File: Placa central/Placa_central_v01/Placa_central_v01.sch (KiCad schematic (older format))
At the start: 69 parts, among them J1 PinoCheckBateriaVcc, J10 Conn_01x01_Arduino11, J11 Conn_01x01_Arduino12, J12 Conn_01x01_Arduino13, J13 Conn_01x01_Arduino14, J14 Conn_01x01_Arduino15, J15 Conn_01x01_Arduino16, J16 Conn_01x01_Motor1PonteHPCB, J17 PinoChargeBateriaGND, J18 Conn_01x01_Arduino19, J19 Conn_01x01_Arduino20, J2 Conn_01x02_ArduinoTxRx, J20 Conn_01x01_Arduino21, J21 Conn_01x01_Arduino22, J22 Conn_01x01_Arduino23, J23 Conn_01x01_Arduino24, J24 Conn_01x01_Arduino25, J25 Conn_01x01_Arduino26, J26 Conn_02x07_IDC_Latch, J27 Conn_01x01_Motor2PonteHPCB, J28 Conn_01x01_Motor1PCBMotor, J29 Conn_01x01_Motor2PCBMotor, J3 Conn_01x01_ArduinoReset, J37 Conn_01x01_8.4VPonteH, J38 Conn_01x01_5VPonteH, J39 Conn_01x01_GNDPonteH, J4 Conn_01x01_Arduino5, J40 Conn_01x01_Motor1PWM, J41 Conn_01x01_Motor1Dir1, J42 Conn_01x01_Motor1Dir2, J43 Conn_01x01_Motor2Dir1, J44 Conn_01x01_Motor2Dir2, J45 Conn_01x01_Motor2PWM, J48 Conn_01x01_5VEncoderEsq, J49 Conn_01x01_OutputEncoderEsq, J5 Conn_01x01_Arduino6, J50 Conn_01x01_GNDEncoderEsq, J51 Conn_01x01_5VEncoderDir, J52 Conn_01x01_OutputEncoderDir, J53 Conn_01x01_GNDEncoderDir, J6 Conn_01x01_Arduino7, J7 Conn_01x01_Arduino8, J8 Conn_01x01_Arduino9, J9 Conn_01x01_Arduino10, Q1 BC548, Q2 BC548, SW1 SW_ON/OFF, SW3 SW_comando1

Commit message: Acertado a placa de sensores
Acertado biblioteca, esquemático, conexão entre as placas e só.
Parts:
- removed J26: Conn_02x07_IDC_Latch, Connector_IDC:IDC-Header_2x07_P2.54mm_Horizontal, symbol Connector_Generic:Conn_02x07_Odd_Even
- added J26: Conn_02x08_Odd_Even, Connector_IDC:IDC-Header_2x08_P2.54mm_Horizontal, symbol Connector_Generic:Conn_02x08_Odd_Even
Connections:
- no-connect marks 6 -> 8
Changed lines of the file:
@@
 Wire Notes Line
 	8700 2550 8700 950
+Text GLabel 4550 2000 0    50   Input ~ 0
+Sensor1
+Text GLabel 4550 1900 0    50   Input ~ 0
+Sensor2
+Text GLabel 4550 1800 0    50   Input ~ 0
+Sensor3
+Text GLabel 4550 1700 0    50   Input ~ 0
+Sensor4
+Text GLabel 4550 1600 0    50   Input ~ 0
+Sensor5
 Text GLabel 4550 1500 0    50   Input ~ 0
-Sensor1
-Text GLabel 4550 1600 0    50   Input ~ 0
-Sensor2
-Text GLabel 4550 1700 0    50   Input ~ 0
-Sensor3
-Text GLabel 4550 1800 0    50   Input ~ 0
-Sensor4
-Text GLabel 4550 1900 0    50   Input ~ 0
-Sensor5
-Text GLabel 5250 1800 2    50   Input ~ 0
 Sensor6
-Text GLabel 5250 1600 2    50   Input ~ 0
+Text GLabel 5250 1900 2    50   Input ~ 0
 Sensor7
+Text GLabel 5250 2100 2    50   Input ~ 0
+SensorEsq
 Text GLabel 5250 1400 2    50   Input ~ 0
-SensorEsq
-Text GLabel 5250 2000 2    50   Input ~ 0
 SensorDir
 Text Notes 4050 2400 0    59   ~ 0
@@
 	0    1    1    0
 $EndComp
-$Comp
-L Connector_Generic:Conn_02x07_Odd_Even J26
-U 1 1 5D1F4EF5
-P 4850 1700
-F 0 "J26" H 4900 2217 50  0000 C CNN
-F 1 "Conn_02x07_IDC_Latch" H 4900 2126 50  0000 C CNN
-F 2 "Connector_IDC:IDC-Header_2x07_P2.54mm_Horizontal" H 4850 1700 50  0001 C CNN
-F 3 "~" H 4850 1700 50  0001 C CNN
-	1    4850 1700
-	1    0    0    -1
-$EndComp
-Text GLabel 4550 1400 0    59   Input ~ 0
+Text GLabel 4550 1400 0    50   Input ~ 0
 GND
 Text GLabel 5000 2600 2    50   Input ~ 0
 VccSensores
-Text GLabel 4550 2000 0    50   Input ~ 0
+Text GLabel 4550 2100 0    50   Input ~ 0
 VccSensores
-Wire Wire Line
-	4550 1400 4650 1400
-Wire Wire Line
-	4550 2000 4650 2000
-Wire Wire Line
-	5250 1400 5150 1400
-Wire Wire Line
-	4550 1500 4650 1500
-Wire Wire Line
-	4650 1600 4550 1600
-Wire Wire Line
-	4550 1700 4650 1700
-Wire Wire Line
-	4550 1800 4650 1800
-Wire Wire Line
-	4550 1900 4650 1900
-Wire Wire Line
-	5150 2000 5250 2000
-Wire Wire Line
-	5150 1800 5250 1800
-Wire Wire Line
-	5150 1600 5250 1600
-NoConn ~ 5150 1500
-NoConn ~ 5150 1700
-NoConn ~ 5150 1900
 Wire Notes Line
 	3700 950  5950 950
@@
 Text Notes 3600 7200 0    39   ~ 0
 Furo da Bateria para fixação na placa:
+$Comp
+L Connector_Generic:Conn_02x08_Odd_Even J26
+U 1 1 5D2D91DB
+P 4850 1700
+F 0 "J26" H 4900 2217 50  0000 C CNN
+F 1 "Conn_02x08_Odd_Even" H 4900 2126 50  0000 C CNN
+F 2 "Connector_IDC:IDC-Header_2x08_P2.54mm_Horizontal" H 4850 1700 50  0001 C CNN
+F 3 "~" H 4850 1700 50  0001 C CNN
+	1    4850 1700
+	1    0    0    -1
+$EndComp
+Wire Wire Line
+	4550 1400 4650 1400
+Wire Wire Line
+	4550 1500 4650 1500
+Wire Wire Line
+	4550 1600 4650 1600
+Wire Wire Line
+	4550 1700 4650 1700
+Wire Wire Line
+	4550 1800 4650 1800
+Wire Wire Line
+	4550 1900 4650 1900
+Wire Wire Line
+	4550 2000 4650 2000
+Wire Wire Line
+	4550 2100 4650 2100
+Wire Wire Line
+	5250 2100 5150 2100
+Wire Wire Line
+	5250 1900 5150 1900
+NoConn ~ 5150 2000
+NoConn ~ 5150 1800
+NoConn ~ 5150 1600
+NoConn ~ 5150 1700
+NoConn ~ 5150 1500
+Wire Wire Line
+	5150 1400 5250 1400
 $EndSCHEMATC

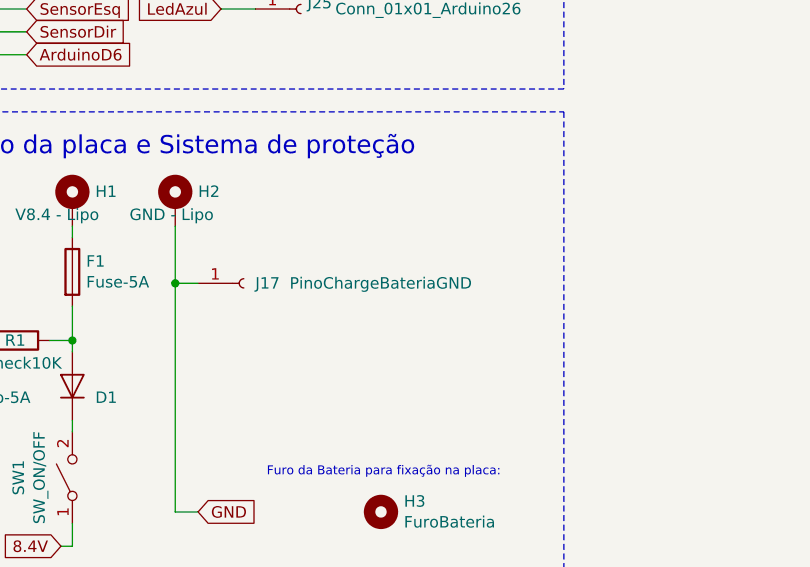
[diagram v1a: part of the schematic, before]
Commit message: Adicionados os componentes à PBC - ainda não posicionados corretamente
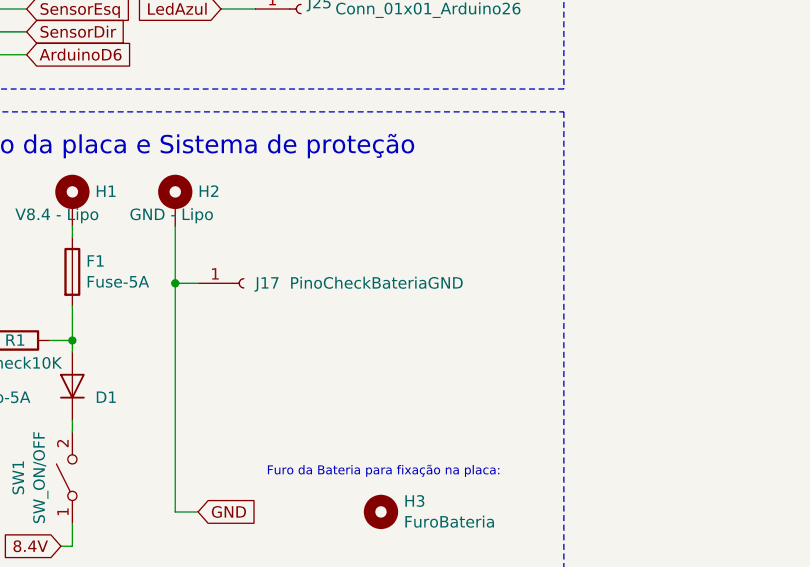
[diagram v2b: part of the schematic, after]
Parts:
- J17: value PinoChargeBateriaGND -> PinoCheckBateriaGND
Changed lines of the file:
@@
 P 3500 6350
 F 0 "J17" H 3550 6350 50  0000 L CNN
-F 1 "PinoChargeBateriaGND" H 3700 6350 50  0000 L CNN
+F 1 "PinoCheckBateriaGND" H 3700 6350 50  0000 L CNN
 F 2 "Connector_Wire:SolderWirePad_1x01_Drill1.5mm" H 3500 6350 50  0001 C CNN
 F 3 "~" H 3500 6350 50  0001 C CNN

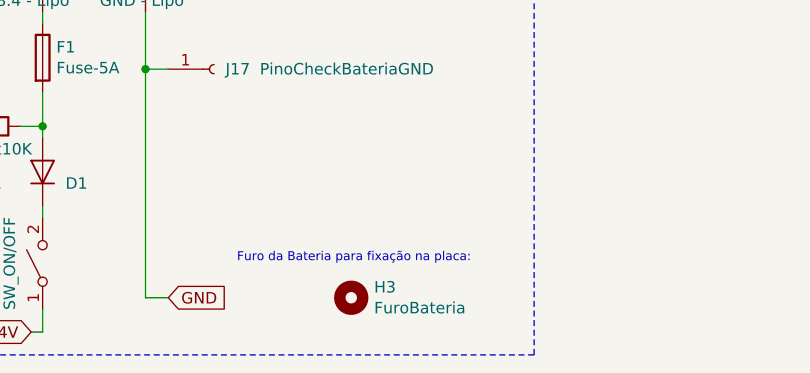
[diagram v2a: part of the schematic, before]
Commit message: Componentes quase todos posicionados, ainda não pronto para root
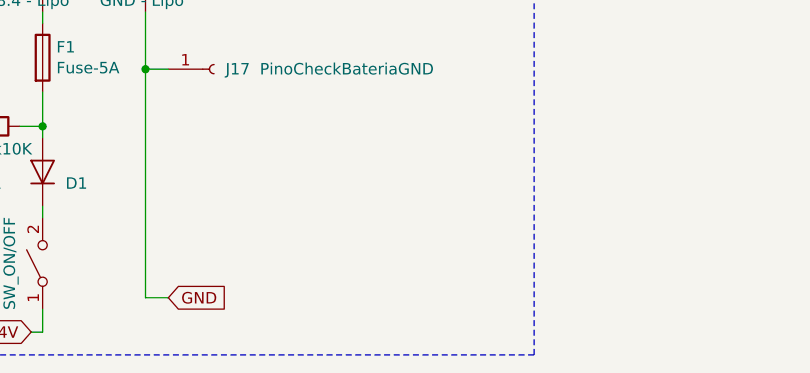
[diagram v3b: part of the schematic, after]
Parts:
- removed H3: FuroBateria, Sensores_e_componentes_SL:Bateria, symbol Mechanical:MountingHole
- J37: footprint Connector_Wire:SolderWirePad_1x01_Drill1.2mm -> Wire_Pads:SolderWirePad_single_1-2mmDrill
- SW1: footprint Sensores_e_componentes_SL:BotaoOnOff -> CUSTOM_Placa_central_v01:Solder_Pad_Custom
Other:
- note removed: "Furo da Bateria para fixação na placa:"
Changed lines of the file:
@@
 F 0 "SW1" H 2750 7435 50  0000 C CNN
 F 1 "SW_ON/OFF" H 2750 7344 50  0000 C CNN
-F 2 "Sensores_e_componentes_SL:BotaoOnOff" H 2750 7200 50  0001 C CNN
+F 2 "CUSTOM_Placa_central_v01:Solder_Pad_Custom" H 2750 7200 50  0001 C CNN
 F 3 "" H 2750 7200 50  0001 C CNN
 	1    2750 7200
@@
 F 0 "J37" H 7228 1276 50  0000 L CNN
 F 1 "Conn_01x01_8.4VPonteH" H 7350 1250 50  0000 L CNN
-F 2 "Connector_Wire:SolderWirePad_1x01_Drill1.2mm" H 7200 1250 50  0001 C CNN
+F 2 "Wire_Pads:SolderWirePad_single_1-2mmDrill" H 7200 1250 50  0001 C CNN
 F 3 "~" H 7200 1250 50  0001 C CNN
 	1    7200 1250
@@
 Furos da PonteH para fixação na placa:
 $Comp
-L Mechanical:MountingHole H3
-U 1 1 5D3C81FB
-P 4100 7350
-F 0 "H3" H 4200 7396 50  0000 L CNN
-F 1 "FuroBateria" H 4200 7305 50  0000 L CNN
-F 2 "Sensores_e_componentes_SL:Bateria" H 4100 7350 50  0001 C CNN
-F 3 "~" H 4100 7350 50  0001 C CNN
-	1    4100 7350
-	1    0    0    -1
-$EndComp
-Text Notes 3600 7200 0    39   ~ 0
-Furo da Bateria para fixação na placa:
-$Comp
 L Connector_Generic:Conn_02x08_Odd_Even J26

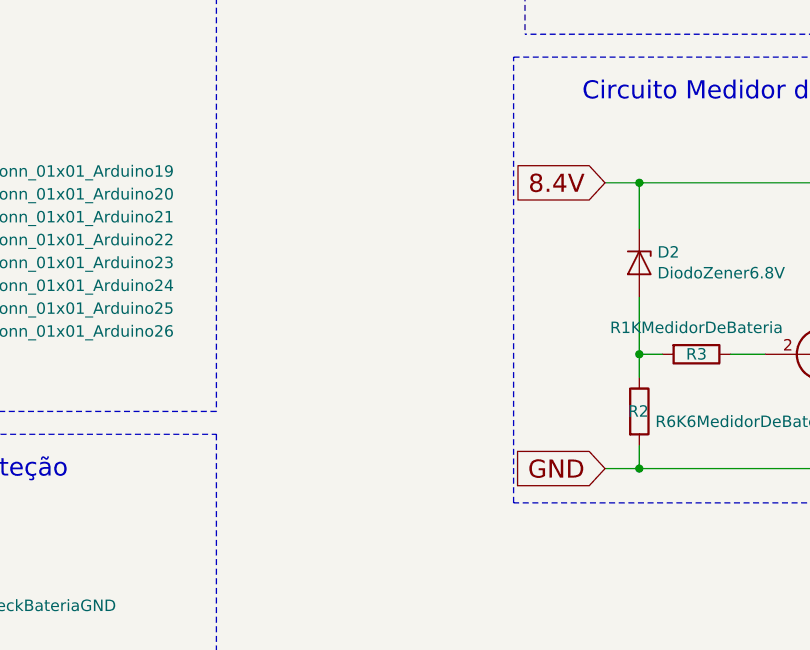
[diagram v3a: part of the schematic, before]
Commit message: Placa auxiliar de alimentacao rooteada, placa central AINDA DESATUALIZADA
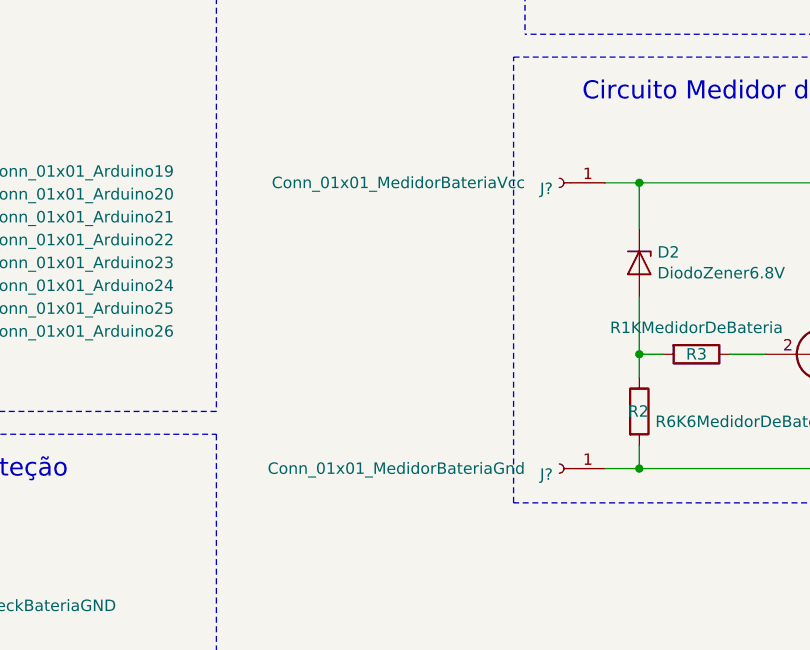
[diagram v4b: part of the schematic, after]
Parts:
- added J?: Conn_01x01_MedidorBateriaVcc, Connector_PinSocket_2.54mm:PinSocket_1x01_P2.54mm_Vertical, symbol Connector:Conn_01x01_Female
- added J?: Conn_01x01_MedidorBateriaGnd, Connector_PinSocket_2.54mm:PinSocket_1x01_P2.54mm_Vertical, symbol Connector:Conn_01x01_Female
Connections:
- net 8.4V: no longer D2.1 (K), R4.1, R5.2
- net GND: no longer Q1.3 (E), Q2.3 (E), R2.2
- new net: D2.1 (K), J?.1 (Pin_1), R4.1, R5.2
- new net: J?.1 (Pin_1), Q1.3 (E), Q2.3 (E), R2.2
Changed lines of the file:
@@
 EESchema Schematic File Version 4
-LIBS:Placa_central_v01-cache
-EELAYER 29 0
+EELAYER 26 0
 EELAYER END
 $Descr A4 11693 8268
@@
 Text GLabel 2850 2950 2    50   Input ~ 0
 LedAzul
-Text GLabel 6600 4500 0    79   Input ~ 0
-8.4V
 $Comp
 L Device:D_Zener D2
@@
 	0    -1   -1   0
 $EndComp
-Text GLabel 6600 5750 0    79   Input ~ 0
-GND
 Wire Wire Line
 	6600 5750 6750 5750
@@
 Wire Wire Line
 	5150 1400 5250 1400
+$Comp
+L Connector:Conn_01x01_Female J?
+U 1 1 5D3D07BC
+P 6400 4500
+F 0 "J?" H 6428 4526 50  0000 L CNN
+F 1 "Conn_01x01_MedidorBateriaVcc" H 6550 4500 50  0000 L CNN
+F 2 "Connector_PinSocket_2.54mm:PinSocket_1x01_P2.54mm_Vertical" H 6400 4500 50  0001 C CNN
+F 3 "~" H 6400 4500 50  0001 C CNN
+	1    6400 4500
+	-1   0    0    1
+$EndComp
+$Comp
+L Connector:Conn_01x01_Female J?
+U 1 1 5D3D515E
+P 6400 5750
+F 0 "J?" H 6428 5776 50  0000 L CNN
+F 1 "Conn_01x01_MedidorBateriaGnd" H 6550 5750 50  0000 L CNN
+F 2 "Connector_PinSocket_2.54mm:PinSocket_1x01_P2.54mm_Vertical" H 6400 5750 50  0001 C CNN
+F 3 "~" H 6400 5750 50  0001 C CNN
+	1    6400 5750
+	-1   0    0    1
+$EndComp
 $EndSCHEMATC

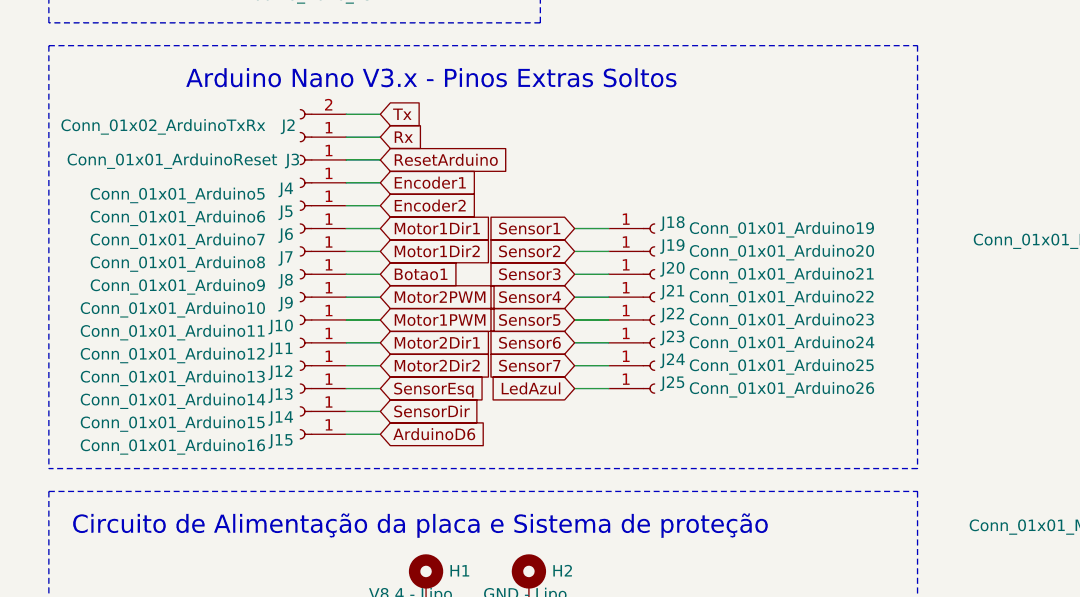
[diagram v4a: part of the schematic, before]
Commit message: Pinos extras removidos
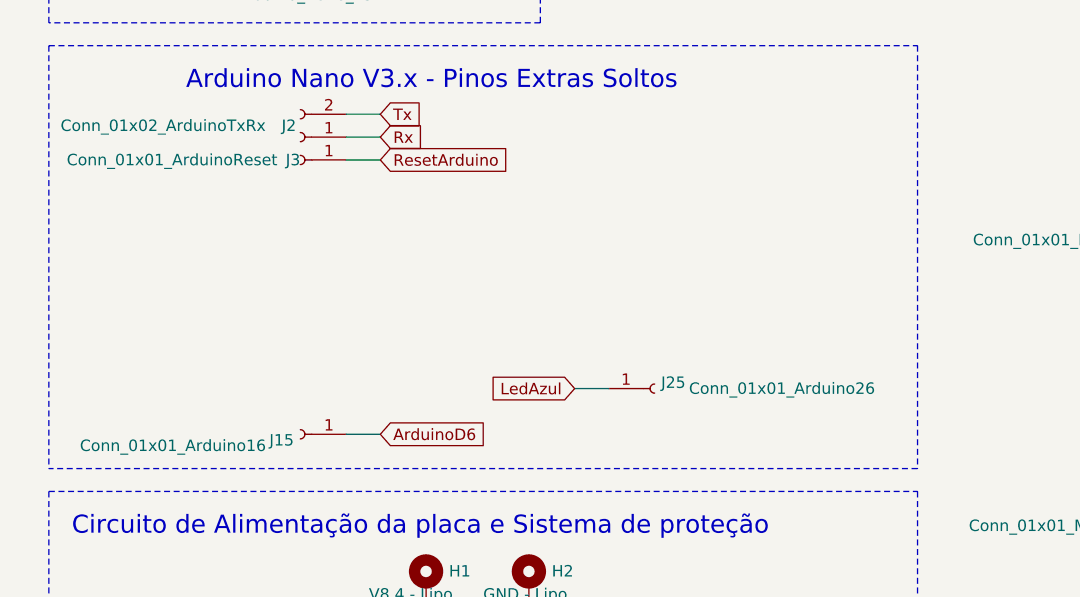
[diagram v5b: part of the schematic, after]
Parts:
- removed J10: Conn_01x01_Arduino11, Connector_PinSocket_2.54mm:PinSocket_1x01_P2.54mm_Vertical, symbol Connector:Conn_01x01_Female
- removed J11: Conn_01x01_Arduino12, Connector_PinSocket_2.54mm:PinSocket_1x01_P2.54mm_Vertical, symbol Connector:Conn_01x01_Female
- removed J12: Conn_01x01_Arduino13, Connector_PinSocket_2.54mm:PinSocket_1x01_P2.54mm_Vertical, symbol Connector:Conn_01x01_Female
- removed J13: Conn_01x01_Arduino14, Connector_PinSocket_2.54mm:PinSocket_1x01_P2.54mm_Vertical, symbol Connector:Conn_01x01_Female
- removed J14: Conn_01x01_Arduino15, Connector_PinSocket_2.54mm:PinSocket_1x01_P2.54mm_Vertical, symbol Connector:Conn_01x01_Female
- removed J18: Conn_01x01_Arduino19, Connector_PinSocket_2.54mm:PinSocket_1x01_P2.54mm_Vertical, symbol Connector:Conn_01x01_Female
- removed J19: Conn_01x01_Arduino20, Connector_PinSocket_2.54mm:PinSocket_1x01_P2.54mm_Vertical, symbol Connector:Conn_01x01_Female
- removed J20: Conn_01x01_Arduino21, Connector_PinSocket_2.54mm:PinSocket_1x01_P2.54mm_Vertical, symbol Connector:Conn_01x01_Female
- removed J21: Conn_01x01_Arduino22, Connector_PinSocket_2.54mm:PinSocket_1x01_P2.54mm_Vertical, symbol Connector:Conn_01x01_Female
- removed J22: Conn_01x01_Arduino23, Connector_PinSocket_2.54mm:PinSocket_1x01_P2.54mm_Vertical, symbol Connector:Conn_01x01_Female
- removed J23: Conn_01x01_Arduino24, Connector_PinSocket_2.54mm:PinSocket_1x01_P2.54mm_Vertical, symbol Connector:Conn_01x01_Female
- removed J24: Conn_01x01_Arduino25, Connector_PinSocket_2.54mm:PinSocket_1x01_P2.54mm_Vertical, symbol Connector:Conn_01x01_Female
- removed J4: Conn_01x01_Arduino5, Connector_PinSocket_2.54mm:PinSocket_1x01_P2.54mm_Vertical, symbol Connector:Conn_01x01_Female
- removed J5: Conn_01x01_Arduino6, Connector_PinSocket_2.54mm:PinSocket_1x01_P2.54mm_Vertical, symbol Connector:Conn_01x01_Female
- removed J6: Conn_01x01_Arduino7, Connector_PinSocket_2.54mm:PinSocket_1x01_P2.54mm_Vertical, symbol Connector:Conn_01x01_Female
- removed J7: Conn_01x01_Arduino8, Connector_PinSocket_2.54mm:PinSocket_1x01_P2.54mm_Vertical, symbol Connector:Conn_01x01_Female
- removed J8: Conn_01x01_Arduino9, Connector_PinSocket_2.54mm:PinSocket_1x01_P2.54mm_Vertical, symbol Connector:Conn_01x01_Female
- removed J9: Conn_01x01_Arduino10, Connector_PinSocket_2.54mm:PinSocket_1x01_P2.54mm_Vertical, symbol Connector:Conn_01x01_Female

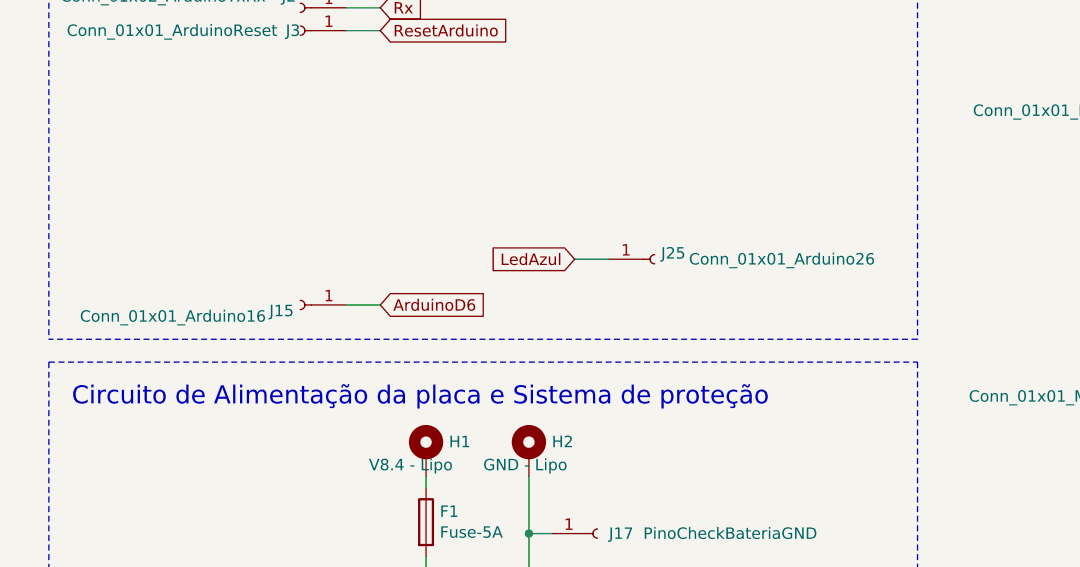
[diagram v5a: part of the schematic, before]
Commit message: Pinos J25(Led Azul) e J15 (ArduinoD6) retirados
Esses pinos serão úteis para futuras expansões, porém suas conexões serão realocadas para o conector principal, e os pinos, para a placa de sensores
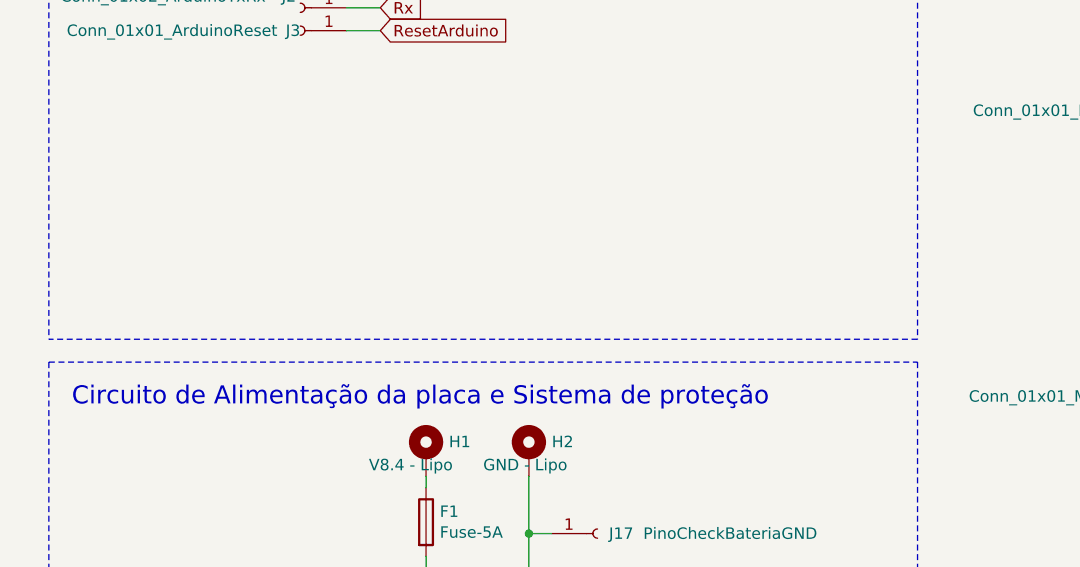
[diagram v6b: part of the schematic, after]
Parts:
- removed J15: Conn_01x01_Arduino16, Connector_PinSocket_2.54mm:PinSocket_1x01_P2.54mm_Vertical, symbol Connector:Conn_01x01_Female
- removed J25: Conn_01x01_Arduino26, Connector_PinSocket_2.54mm:PinSocket_1x01_P2.54mm_Vertical, symbol Connector:Conn_01x01_Female
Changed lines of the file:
@@
 Text GLabel 1650 2950 0    50   Input ~ 0
 Botao1
-Text GLabel 3400 5150 0    50   Input ~ 0
-LedAzul
 Text GLabel 3300 7350 2    50   Input ~ 0
 GND
@@
 	2750 6650 2750 6600
 Connection ~ 2750 6600
-$Comp
-L Connector:Conn_01x01_Female J15
-U 1 1 5D2129B1
-P 2200 5350
-F 0 "J15" H 2228 5376 50  0000 L CNN
-F 1 "Conn_01x01_Arduino16" H 2350 5400 50  0000 L CNN
-F 2 "Connector_PinSocket_2.54mm:PinSocket_1x01_P2.54mm_Vertical" H 2200 5350 50  0001 C CNN
-F 3 "~" H 2200 5350 50  0001 C CNN
-	1    2200 5350
-	-1   0    0    1
-$EndComp
-$Comp
-L Connector:Conn_01x01_Female J25
-U 1 1 5D21B22A
-P 3750 5150
-F 0 "J25" H 3778 5176 50  0000 L CNN
-F 1 "Conn_01x01_Arduino26" H 3900 5150 50  0000 L CNN
-F 2 "Connector_PinSocket_2.54mm:PinSocket_1x01_P2.54mm_Vertical" H 3750 5150 50  0001 C CNN
-F 3 "~" H 3750 5150 50  0001 C CNN
-	1    3750 5150
-	1    0    0    -1
-$EndComp
-Text GLabel 2550 5350 2    50   Input ~ 0
-ArduinoD6
-Wire Wire Line
-	3400 5150 3550 5150
-Wire Wire Line
-	2400 5350 2550 5350
 Text Notes 1700 3850 0    79   ~ 0
 Arduino Nano V3.x - Pinos Extras Soltos
